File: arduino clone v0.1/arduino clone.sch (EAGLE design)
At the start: 17 parts, among them U101 ATMEGA328P_TQFP, U201 CH340G

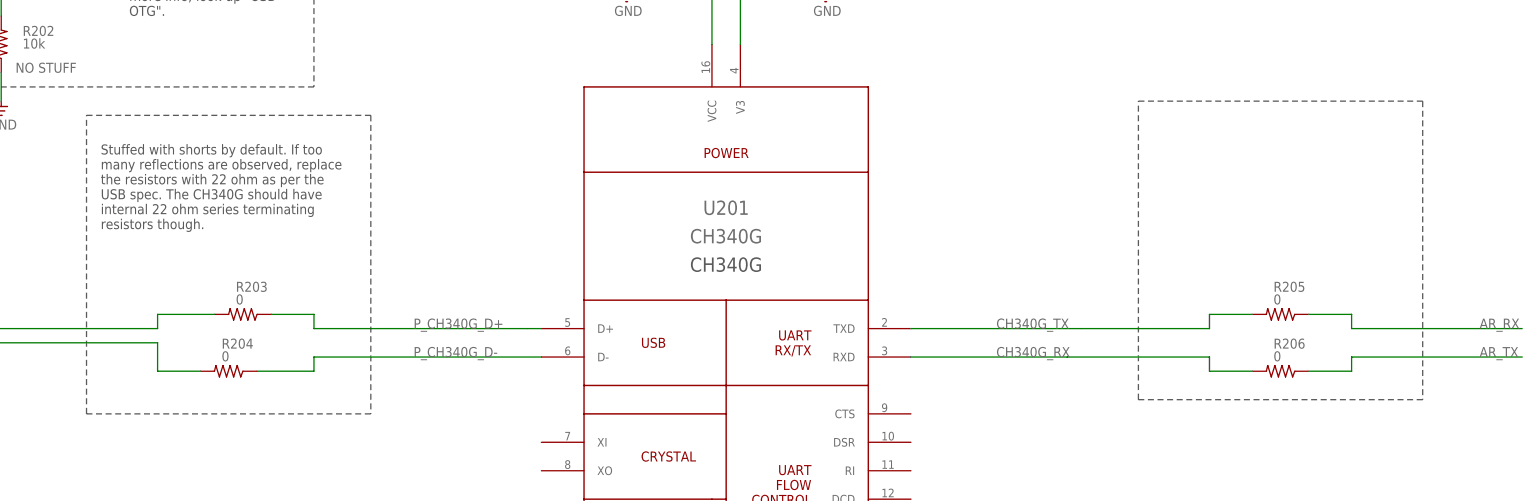
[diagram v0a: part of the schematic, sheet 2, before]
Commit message: Add note for series resistors on RX and TX lines UART
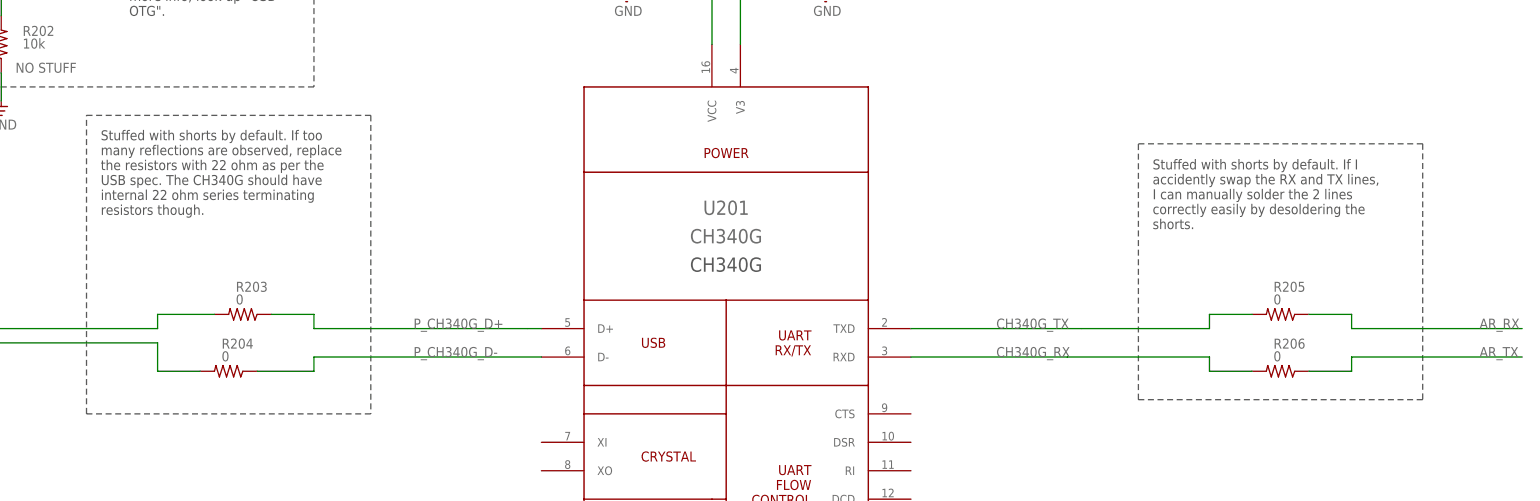
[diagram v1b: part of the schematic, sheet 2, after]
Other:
- note added: "Stuffed with shorts by default. If I accidently swap the RX and TX lines, I can manually solder the 2 lines correctly easily by desoldering the shorts."
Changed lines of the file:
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@@
 <wire x1="142.24" y1="104.14" x2="91.44" y2="104.14" width="0.1524" layer="97" style="shortdash"/>
 <wire x1="91.44" y1="104.14" x2="91.44" y2="157.48" width="0.1524" layer="97" style="shortdash"/>
-<text x="93.98" y="137.16" size="1.778" layer="97">Stuffed with shorts by default. If too
+<text x="93.98" y="139.7" size="1.778" layer="97">Stuffed with shorts by default. If too
 many reflections are observed, replace
 the resistors with 22 ohm as per the
@@
 internal 22 ohm series terminating
 resistors though.</text>
-<wire x1="279.4" y1="160.02" x2="330.2" y2="160.02" width="0.1524" layer="97" style="shortdash"/>
-<wire x1="330.2" y1="160.02" x2="330.2" y2="106.68" width="0.1524" layer="97" style="shortdash"/>
+<wire x1="279.4" y1="152.4" x2="330.2" y2="152.4" width="0.1524" layer="97" style="shortdash"/>
+<wire x1="330.2" y1="152.4" x2="330.2" y2="106.68" width="0.1524" layer="97" style="shortdash"/>
 <wire x1="330.2" y1="106.68" x2="279.4" y2="106.68" width="0.1524" layer="97" style="shortdash"/>
-<wire x1="279.4" y1="106.68" x2="279.4" y2="160.02" width="0.1524" layer="97" style="shortdash"/>
+<wire x1="279.4" y1="106.68" x2="279.4" y2="152.4" width="0.1524" layer="97" style="shortdash"/>
+<text x="281.94" y="137.16" size="1.778" layer="97">Stuffed with shorts by default. If I
+accidently swap the RX and TX lines,
+I can manually solder the 2 lines
+correctly easily by desoldering the
+shorts.</text>
 </plain>
 <instances>

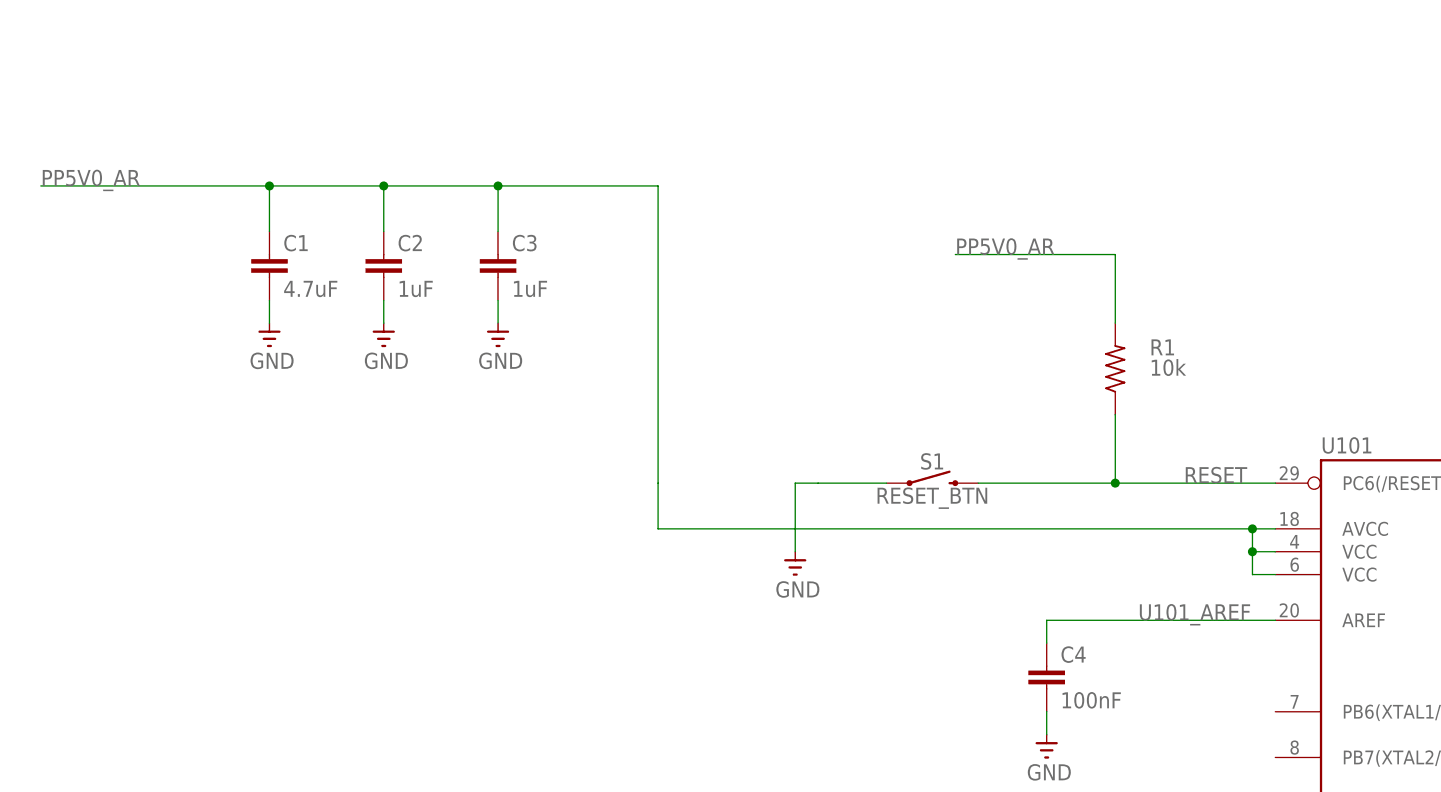
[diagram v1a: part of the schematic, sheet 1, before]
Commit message: rename MCU nets to have 'mcu'
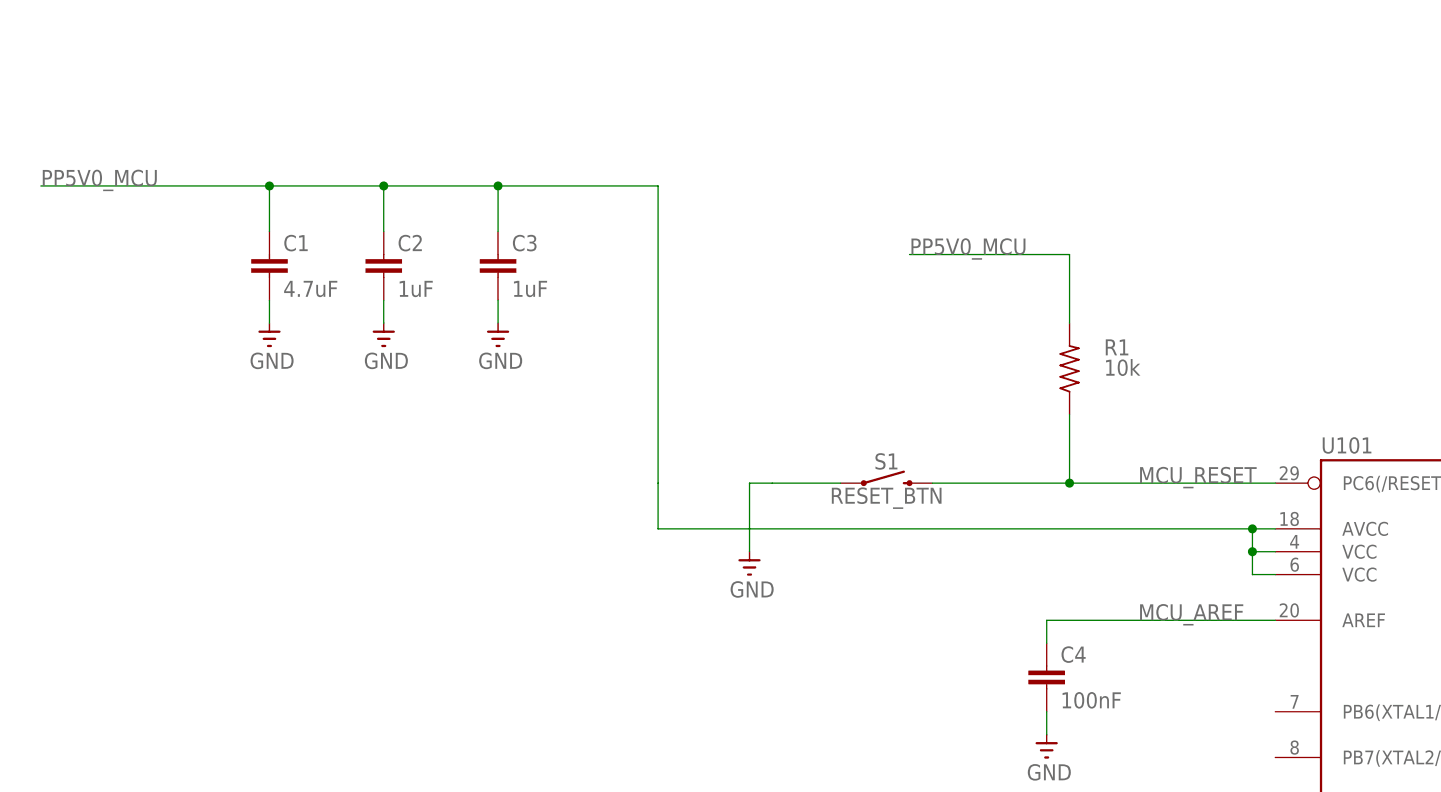
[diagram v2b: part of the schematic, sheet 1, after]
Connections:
- net PP5V0_AR renamed PP5V0_MCU
- net RESET renamed MCU_RESET
- net U101_AREF renamed MCU_AREF
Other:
- moved on the sheet: R1, S1
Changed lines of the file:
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@@
 <attribute name="VALUE" x="79.0575" y="175.26" size="1.778" layer="96"/>
 </instance>
-<instance part="R1" gate="G$1" x="149.86" y="175.26" smashed="yes" rot="R90">
-<attribute name="NAME" x="153.67" y="176.7586" size="1.778" layer="95"/>
-<attribute name="VALUE" x="153.67" y="174.498" size="1.778" layer="96"/>
+<instance part="R1" gate="G$1" x="144.78" y="175.26" smashed="yes" rot="R90">
+<attribute name="NAME" x="148.59" y="176.7586" size="1.778" layer="95"/>
+<attribute name="VALUE" x="148.59" y="174.498" size="1.778" layer="96"/>
 </instance>
 <instance part="C4" gate="G$1" x="142.24" y="142.24"/>
@@
 <attribute name="VALUE" x="140.0175" y="129.54" size="1.778" layer="96"/>
 </instance>
-<instance part="S1" gate="G$1" x="129.54" y="162.56"/>
-<instance part="GND6" gate="1" x="114.3" y="152.4" smashed="yes">
-<attribute name="VALUE" x="112.0775" y="149.86" size="1.778" layer="96"/>
+<instance part="S1" gate="G$1" x="124.46" y="162.56"/>
+<instance part="GND6" gate="1" x="109.22" y="152.4" smashed="yes">
+<attribute name="VALUE" x="106.9975" y="149.86" size="1.778" layer="96"/>
 </instance>
 </instances>
@@
 </busses>
 <nets>
-<net name="PP5V0_AR" class="0">
+<net name="PP5V0_MCU" class="0">
 <segment>
 <label x="30.48" y="195.58" size="1.778" layer="95"/>
@@
 <segment>
 <pinref part="R1" gate="G$1" pin="2"/>
-<wire x1="149.86" y1="180.34" x2="149.86" y2="187.96" width="0.1524" layer="91"/>
-<wire x1="149.86" y1="187.96" x2="132.08" y2="187.96" width="0.1524" layer="91"/>
-<label x="132.08" y="187.96" size="1.778" layer="95"/>
+<wire x1="144.78" y1="180.34" x2="144.78" y2="187.96" width="0.1524" layer="91"/>
+<wire x1="144.78" y1="187.96" x2="127" y2="187.96" width="0.1524" layer="91"/>
+<label x="127" y="187.96" size="1.778" layer="95"/>
 </segment>
 </net>
@@
 <segment>
 <pinref part="GND6" gate="1" pin="GND"/>
-<wire x1="114.3" y1="154.94" x2="114.3" y2="162.56" width="0.1524" layer="91"/>
-<wire x1="114.3" y1="162.56" x2="116.84" y2="162.56" width="0.1524" layer="91"/>
+<wire x1="109.22" y1="154.94" x2="109.22" y2="162.56" width="0.1524" layer="91"/>
+<wire x1="109.22" y1="162.56" x2="111.76" y2="162.56" width="0.1524" layer="91"/>
 <pinref part="S1" gate="G$1" pin="1"/>
-<wire x1="116.84" y1="162.56" x2="124.46" y2="162.56" width="0.1524" layer="91"/>
+<wire x1="111.76" y1="162.56" x2="119.38" y2="162.56" width="0.1524" layer="91"/>
 </segment>
 </net>
-<net name="RESET" class="0">
+<net name="MCU_RESET" class="0">
 <segment>
 <pinref part="R1" gate="G$1" pin="1"/>
-<wire x1="149.86" y1="170.18" x2="149.86" y2="162.56" width="0.1524" layer="91"/>
+<wire x1="144.78" y1="170.18" x2="144.78" y2="162.56" width="0.1524" layer="91"/>
 <pinref part="U101" gate="U$1" pin="PC6(/RESET)"/>
-<wire x1="149.86" y1="162.56" x2="167.64" y2="162.56" width="0.1524" layer="91"/>
-<label x="157.48" y="162.56" size="1.778" layer="95"/>
+<wire x1="144.78" y1="162.56" x2="167.64" y2="162.56" width="0.1524" layer="91"/>
+<label x="152.4" y="162.56" size="1.778" layer="95"/>
 <pinref part="S1" gate="G$1" pin="2"/>
-<wire x1="134.62" y1="162.56" x2="149.86" y2="162.56" width="0.1524" layer="91"/>
-<junction x="149.86" y="162.56"/>
+<wire x1="129.54" y1="162.56" x2="144.78" y2="162.56" width="0.1524" layer="91"/>
+<junction x="144.78" y="162.56"/>
 </segment>
 </net>
-<net name="U101_AREF" class="0">
+<net name="MCU_AREF" class="0">
 <segment>
 <pinref part="C4" gate="G$1" pin="1"/>

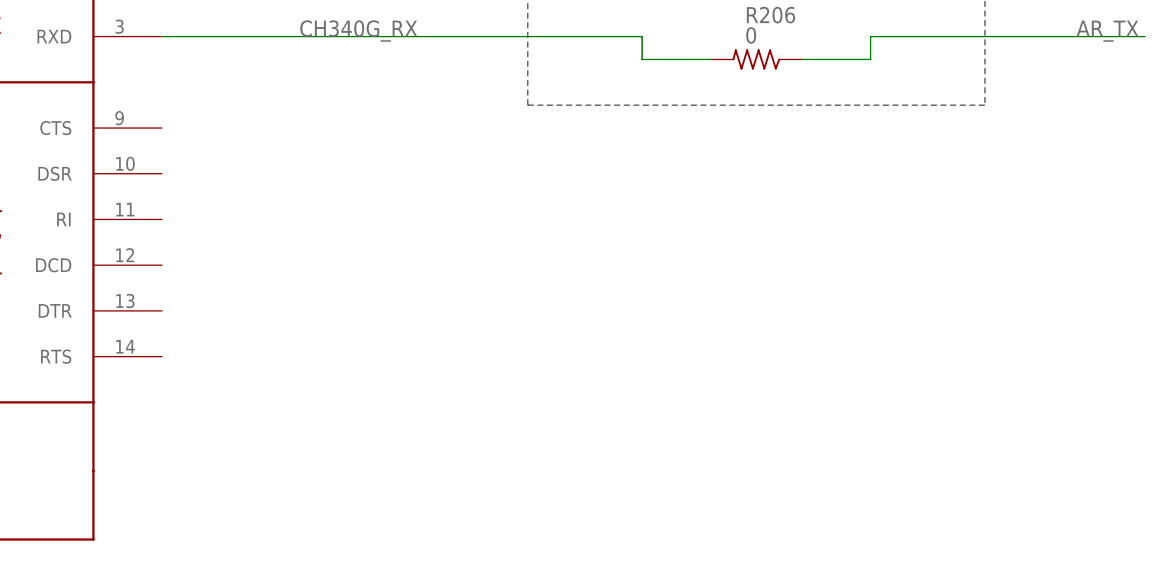
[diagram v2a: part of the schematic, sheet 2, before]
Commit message: add AC coupling cap on DTR line of CH340G
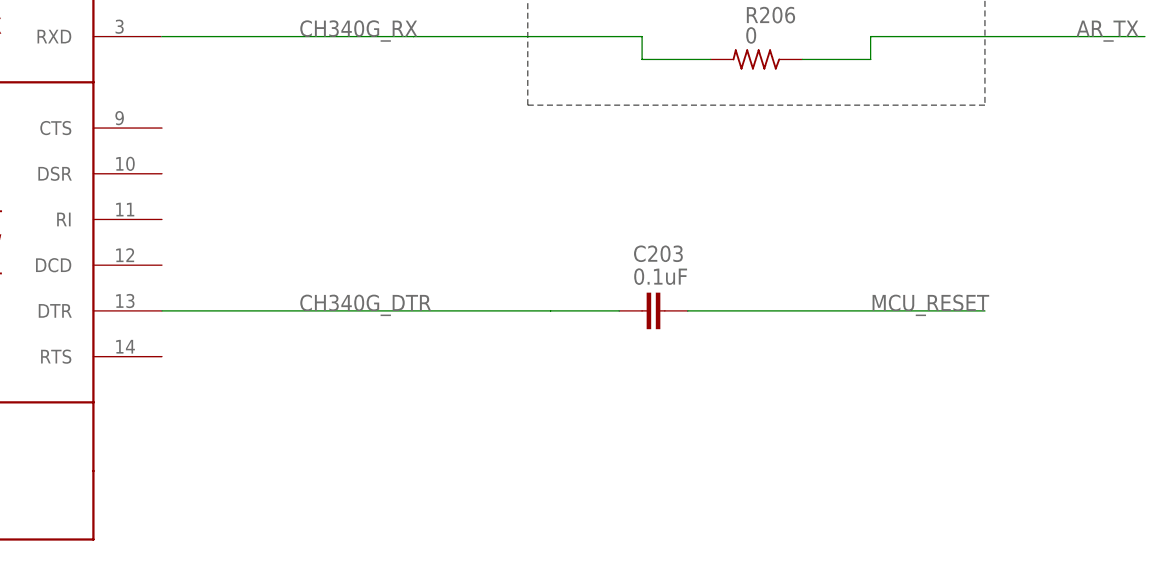
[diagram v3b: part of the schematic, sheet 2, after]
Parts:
- added C203: 0.1uF, rcl:C-EUC0805
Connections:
- new net CH340G_DTR: C203.1, U201.DTR
- net MCU_RESET: now also C203.2
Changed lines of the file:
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@@
 <part name="R205" library="adafruit" deviceset="R-US_" device="R0805" value="0"/>
 <part name="R206" library="adafruit" deviceset="R-US_" device="R0805" value="0"/>
+<part name="C203" library="rcl" library_urn="urn:adsk.eagle:library:334" deviceset="C-EU" device="C0805" package3d_urn="urn:adsk.eagle:package:23617/2" value="0.1uF"/>
 </parts>
 <sheets>
@@
 <attribute name="VALUE" x="303.53" y="113.538" size="1.778" layer="96"/>
 </instance>
+<instance part="C203" gate="G$1" x="292.1" y="83.82" smashed="yes" rot="R90">
+<attribute name="NAME" x="291.084" y="89.281" size="1.778" layer="95"/>
+<attribute name="VALUE" x="291.084" y="86.741" size="1.778" layer="96"/>
+</instance>
 </instances>
 <busses>
@@
 </segment>
 </net>
+<net name="CH340G_DTR" class="0">
+<segment>
+<pinref part="U201" gate="G$1" pin="DTR"/>
+<wire x1="238.76" y1="83.82" x2="281.94" y2="83.82" width="0.1524" layer="91"/>
+<pinref part="C203" gate="G$1" pin="1"/>
+<wire x1="281.94" y1="83.82" x2="289.56" y2="83.82" width="0.1524" layer="91"/>
+<label x="254" y="83.82" size="1.778" layer="95"/>
+</segment>
+</net>
+<net name="MCU_RESET" class="0">
+<segment>
+<pinref part="C203" gate="G$1" pin="2"/>
+<wire x1="297.18" y1="83.82" x2="330.2" y2="83.82" width="0.1524" layer="91"/>
+<label x="317.5" y="83.82" size="1.778" layer="95"/>
+</segment>
+</net>
